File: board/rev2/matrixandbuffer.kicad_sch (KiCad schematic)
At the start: 2 parts, among them J4 Conn_02x08_Counter_Clockwise, U12 74HC245

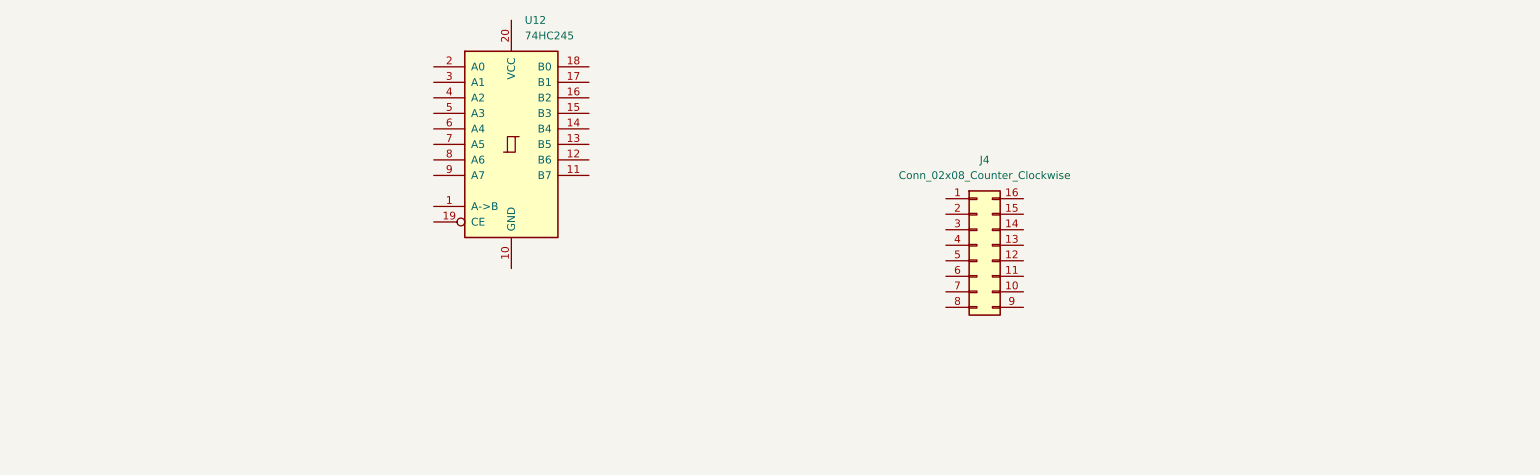
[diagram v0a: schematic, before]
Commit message: Continue board work
- move to rp2040, separate stm32g071 to do usb-c + aux ctrl IO
  - still cheaper lol with the cost of stm32s
- more power reg stuff
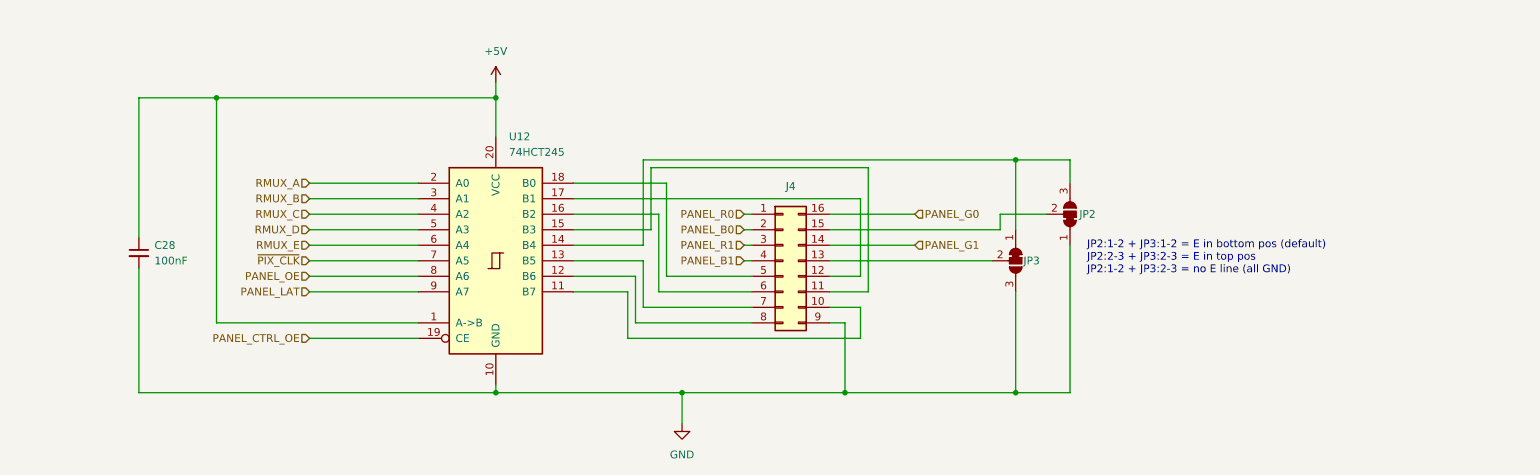
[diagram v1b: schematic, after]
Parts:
- added C28: 100nF, symbol Device:C_Small
- added JP2, JP3: SolderJumper_3_Bridged12, symbol Jumper:SolderJumper_3_Bridged12
- U12: value 74HC245 -> 74HCT245
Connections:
- net +5V: now reaches U12.1 (A->B)
- net +5V: now also U12.20 (VCC), C28.1
- net GND: now reaches U12.10 (GND)
- net GND: now also J4.9 (Pin_9), C28.2, JP2.1 (A), JP3.3 (B)
- net at U12.11 (B7): now also J4.10 (Pin_10)
- net at U12.12 (B6): now also J4.8 (Pin_8)
- net at U12.13 (B5): now also J4.7 (Pin_7)
- net at U12.14 (B4): now also JP2.3 (B), JP3.1 (A)
- net at U12.15 (B3): now also J4.11 (Pin_11)
- net at U12.16 (B2): now also J4.6 (Pin_6)
- net at U12.17 (B1): now also J4.12 (Pin_12)
- net at U12.18 (B0): now also J4.5 (Pin_5)
- net PANEL_CTRL_OE: now reaches U12.19 (CE)
- net RMUX_A: now reaches U12.2 (A0)
- net RMUX_B: now reaches U12.3 (A1)
- net RMUX_C: now reaches U12.4 (A2)
- net RMUX_D: now reaches U12.5 (A3)
- net RMUX_E: now reaches U12.6 (A4)
- net ~{PIX_CLK}: now reaches U12.7 (A5)
- net PANEL_OE: now reaches U12.8 (A6)
- net PANEL_LAT: now reaches U12.9 (A7)
- net PANEL_R0: now reaches J4.1 (Pin_1)
- net at J4.13 (Pin_13): now also JP3.2 (C)
- net PANEL_G1: now reaches J4.14 (Pin_14)
- net at J4.15 (Pin_15): now also JP2.2 (C)
- net PANEL_G0: now reaches J4.16 (Pin_16)
- net PANEL_B0: now reaches J4.2 (Pin_2)
- net PANEL_R1: now reaches J4.3 (Pin_3)
- net PANEL_B1: now reaches J4.4 (Pin_4)
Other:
- note added: "JP2:1-2 + JP3:1-2 = E in bottom pos (default) JP2:2-3 + JP3:2-3 = E in top pos JP2:1-2 + JP3:2-3 = no E line (all GND)"
- moved on the sheet: J4, U12

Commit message: Split out board into A/B
allow 2x displays (for chaining)
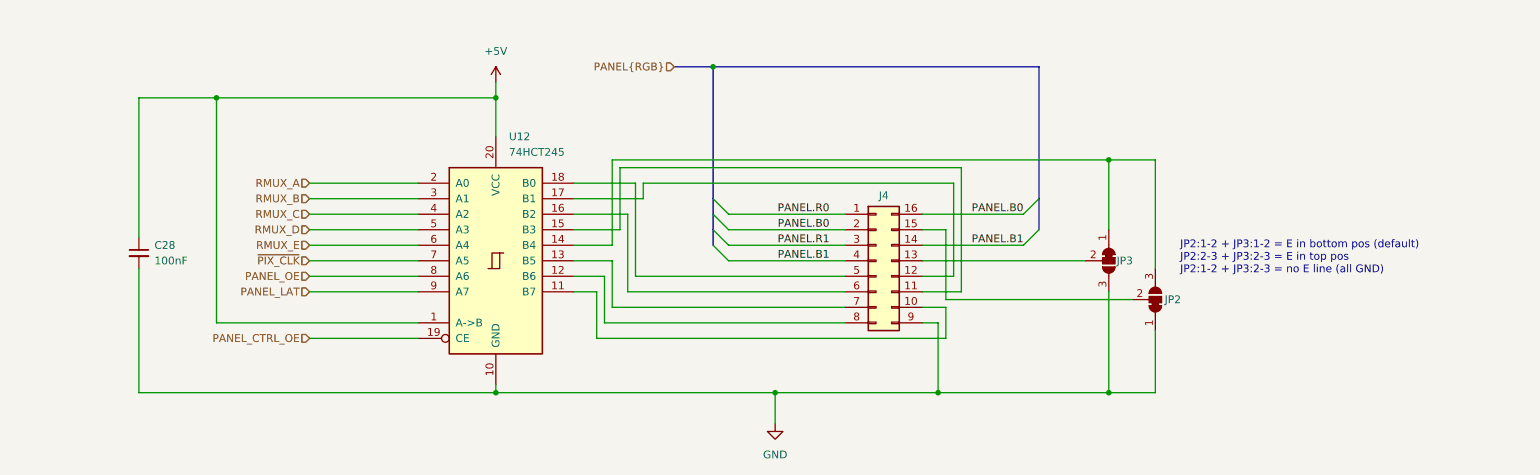
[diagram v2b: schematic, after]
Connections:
- net PANEL_G0 is gone; now on net PANEL.B0: J4.16 (Pin_16)
- net PANEL_G1 is gone; now on net PANEL.B1: J4.14 (Pin_14)
- net PANEL_B0 renamed PANEL.B0
- net PANEL_B1 renamed PANEL.B1
- net PANEL_R0 renamed PANEL.R0
- net PANEL_R1 renamed PANEL.R1
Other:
- moved on the sheet: J4, JP2, JP3

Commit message: More board work
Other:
- note removed: "JP2:1-2 + JP3:1-2 = E in bottom pos (default) JP2:2-3 + JP3:2-3 = E in top pos JP2:1-2 + JP3:2-3 = no E line (all GND)"
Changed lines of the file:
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@@
 	(generator_version "9.0")
 	(paper "A4")
-	(text "JP2:1-2 + JP3:1-2 = E in bottom pos (default)\nJP2:2-3 + JP3:2-3 = E in top pos\nJP2:1-2 + JP3:2-3 = no E line (all GND)"
-		(exclude_from_sim no)
-		(at 228.854 98.552 0)
-		(effects
-			(font
-				(size 1.27 1.27)
-			)
-			(justify left)
-		)
-	)
 	(junction
 		(at 162.56 120.65)
@@
 		)
 	)
+	(table
+		(column_count 3)
+		(border
+			(external yes)
+			(header yes)
+			(stroke
+				(width 0)
+				(type solid)
+			)
+		)
+		(separators
+			(rows no)
+			(cols yes)
+			(stroke
+				(width 0)
+				(type solid)
+			)
+		)
+		(column_widths 12.7 10.16 20.32)
+		(row_heights 2.54 2.54 2.54 2.54)
+		(cells
+			(table_cell "JP2"
+				(exclude_from_sim no)
+				(at 232.41 96.52 0)
+				(size 12.7 2.54)
+				(margins 0.9525 0.9525 0.9525 0.9525)
+				(span 1 1)
+				(fill
+					(type none)
+				)
+				(effects
+					(font
+						(size 1.27 1.27)
+						(thickness 0.254)
+						(bold yes)
+					)
+					(justify top)
+				)
+			)
+			(table_cell "JP3"
+				(exclude_from_sim no)
+				(at 245.11 96.52 0)
+				(size 10.16 2.54)
+				(margins 0.9525 0.9525 0.9525 0.9525)
+				(span 1 1)
+				(fill
+					(type none)
+				)
+				(effects
+					(font
+						(size 1.27 1.27)
+						(thickness 0.254)
+						(bold yes)
+					)
+					(justify top)
+				)
+			)
+			(table_cell ""
+				(exclude_from_sim no)
+				(at 255.27 96.52 0)
+				(size 20.32 2.54)
+				(margins 0.9525 0.9525 0.9525 0.9525)
+				(span 1 1)
+				(fill
+					(type color)
+					(color 255 255 194 1)
+				)
+				(effects
+					(font
+						(size 1.27 1.27)
+					)
+					(justify left top)
+				)
+			)
+			(table_cell "default"
+				(exclude_from_sim no)
+				(at 232.41 99.06 0)
+				(size 12.7 2.54)
+				(margins 0.9525 0.9525 0.9525 0.9525)
+				(span 1 1)
+				(fill
+					(type none)
+				)
+				(effects
+					(font
+						(size 1.27 1.27)
+					)
+					(justify left top)
+				)
+			)
+			(table_cell "default"
+				(exclude_from_sim no)
+				(at 245.11 99.06 0)
+				(size 10.16 2.54)
+				(margins 0.9525 0.9525 0.9525 0.9525)
+				(span 1 1)
+				(fill
+					(type none)
+				)
+				(effects
+					(font
+						(size 1.27 1.27)
+					)
+					(justify left top)
+				)
+			)
+			(table_cell "E on bottom"
+				(exclude_from_sim no)
+				(at 255.27 99.06 0)
+				(size 20.32 2.54)
+				(margins 0.9525 0.9525 0.9525 0.9525)
+				(span 1 1)
+				(fill
+					(type none)
+				)
+				(effects
+					(font
+						(size 1.27 1.27)
+					)
+					(justify left top)
+				)
+			)
+			(table_cell "cut"
+				(exclude_from_sim no)
+				(at 232.41 101.6 0)
+				(size 12.7 2.54)
+				(margins 0.9525 0.9525 0.9525 0.9525)
+				(span 1 1)
+				(fill
+					(type none)
+				)
+				(effects
+					(font
+						(size 1.27 1.27)
+					)
+					(justify left top)
+				)
+			)
+			(table_cell "cut"
+				(exclude_from_sim no)
+				(at 245.11 101.6 0)
+				(size 10.16 2.54)
+				(margins 0.9525 0.9525 0.9525 0.9525)
+				(span 1 1)
+				(fill
+					(type none)
+				)
+				(effects
+					(font
+						(size 1.27 1.27)
+					)
+					(justify left top)
+				)
+			)
+			(table_cell "E on top"
+				(exclude_from_sim no)
+				(at 255.27 101.6 0)
+				(size 20.32 2.54)
+				(margins 0.9525 0.9525 0.9525 0.9525)
+				(span 1 1)
+				(fill
+					(type none)
+				)
+				(effects
+					(font
+						(size 1.27 1.27)
+					)
+					(justify left top)
+				)
+			)
+			(table_cell "default"
+				(exclude_from_sim no)
+				(at 232.41 104.14 0)
+				(size 12.7 2.54)
+				(margins 0.9525 0.9525 0.9525 0.9525)
+				(span 1 1)
+				(fill
+					(type none)
+				)
+				(effects
+					(font
+						(size 1.27 1.27)
+					)
+					(justify left top)
+				)
+			)
+			(table_cell "cut"
+				(exclude_from_sim no)
+				(at 245.11 104.14 0)
+				(size 10.16 2.54)
+				(margins 0.9525 0.9525 0.9525 0.9525)
+				(span 1 1)
+				(fill
+					(type none)
+				)
+				(effects
+					(font
+						(size 1.27 1.27)
+					)
+					(justify left top)
+				)
+			)
+			(table_cell "both choices GND"
+				(exclude_from_sim no)
+				(at 255.27 104.14 0)
+				(size 20.32 2.54)
+				(margins 0.9525 0.9525 0.9525 0.9525)
+				(span 1 1)
+				(fill
+					(type none)
+				)
+				(effects
+					(font
+						(size 1.27 1.27)
+					)
+					(justify left top)
+				)
+			)
+		)
+	)

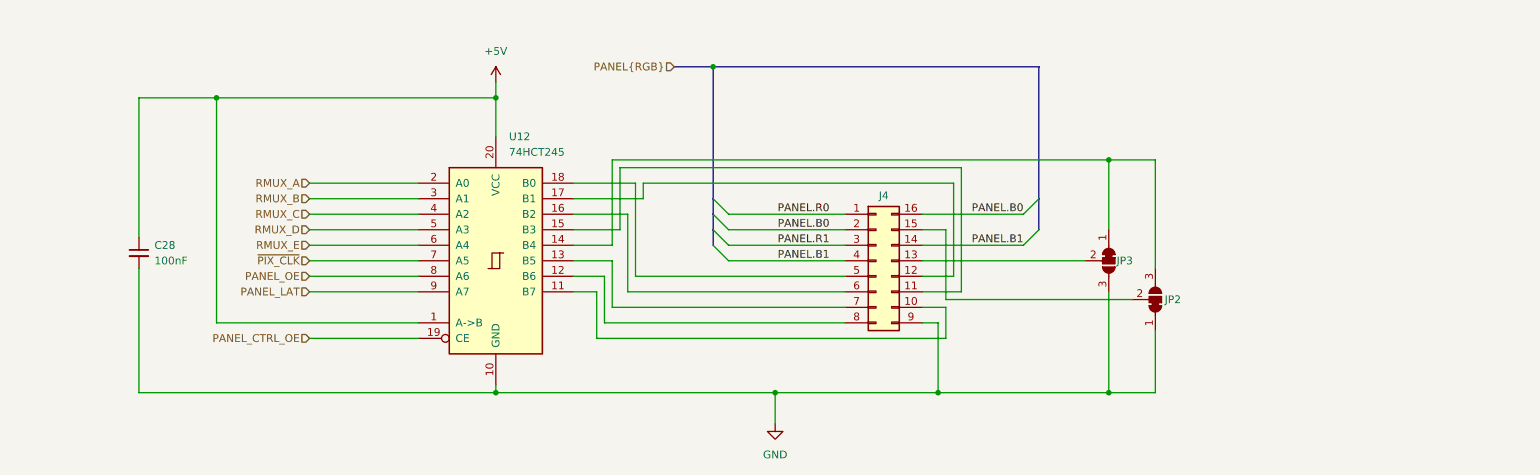
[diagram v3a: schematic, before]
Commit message: Board GPIO allocation
- and usbmux

still need to do termination on the big buses + a bunch of bypass caps
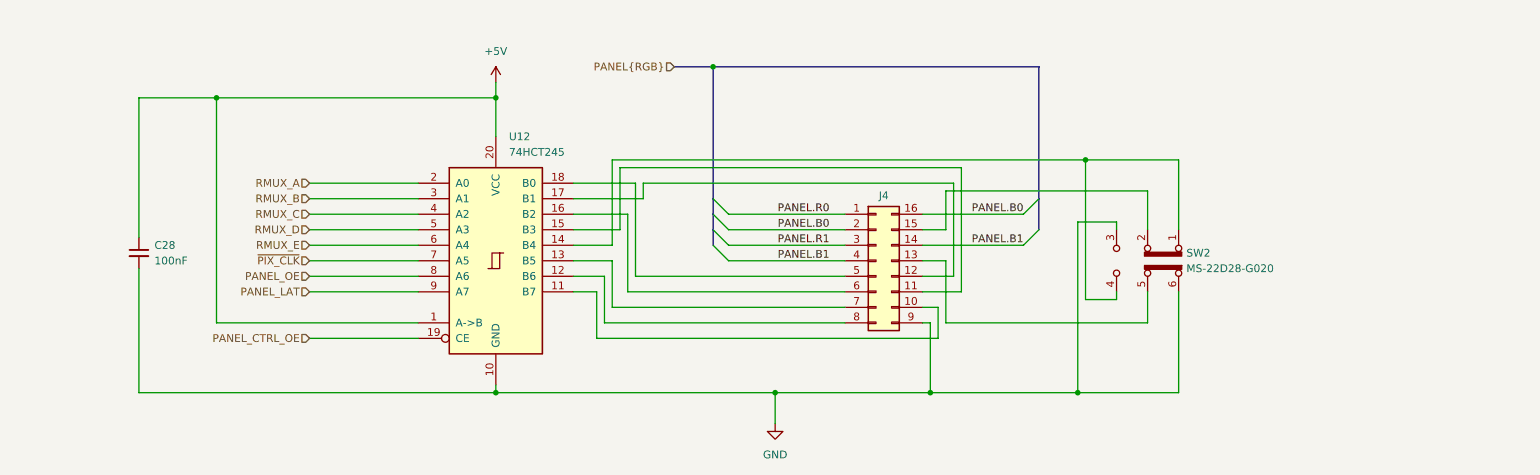
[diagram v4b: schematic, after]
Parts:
- removed JP2, JP3: SolderJumper_3_Bridged12, symbol Jumper:SolderJumper_3_Bridged12
- added SW2: MS-22D28-G020, symbol Switch:SW_Slide_DPDT
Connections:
- net GND: now also SW2.3 (C), SW2.6 (C)
- net at J4.15 (Pin_15): now also SW2.2 (B)
- net at U12.14 (B4): now also SW2.1 (A), SW2.4 (A)
- net at J4.13 (Pin_13): now also SW2.5 (B)
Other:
- company: (none) -> MLABS
- title: (none) -> LED Level Shifter + Socket

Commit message: Continue board, assign caps/res, adjust for JLC availability
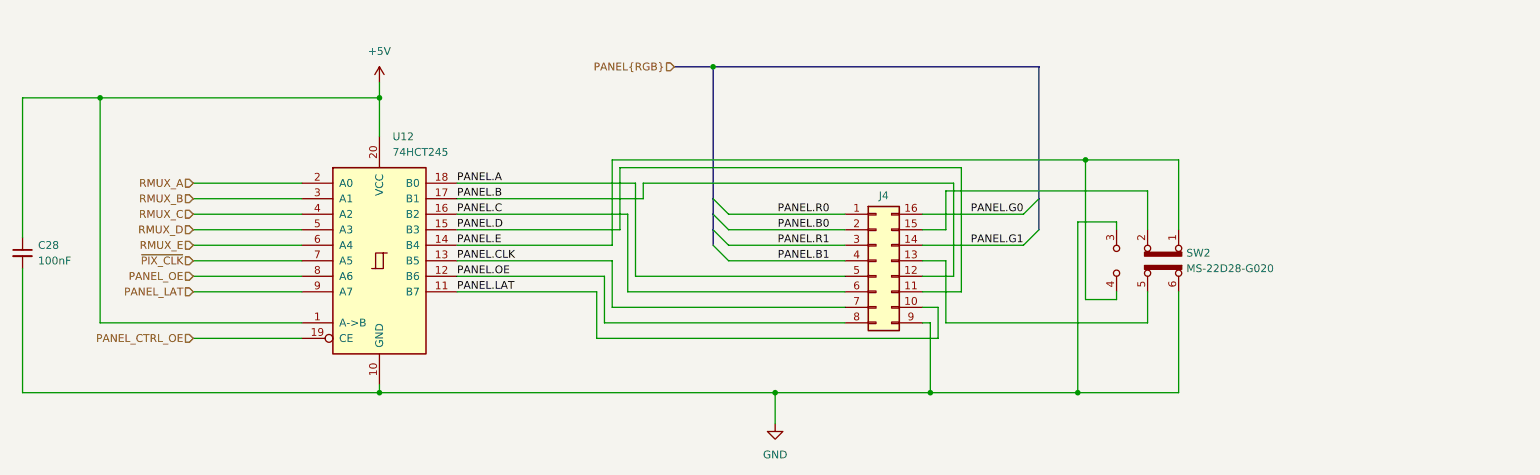
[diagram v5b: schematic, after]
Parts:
- C28: footprint (none) -> Capacitor_SMD:C_0402_1005Metric; Part (none) -> CL05B104KB54PNC
- J4: footprint (none) -> Connector_IDC:IDC-Header_2x07_P2.54mm_Vertical
- U12: footprint (none) -> Package_SO:TSSOP-20-1EP_4.4x6.5mm_P0.65mm_EP2.15x3.35mm
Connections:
- net PANEL.B0: no longer J4.16 (Pin_16)
- net PANEL.B1: no longer J4.14 (Pin_14)
- net PANEL.LAT: now reaches J4.10 (Pin_10), U12.11 (B7)
- net PANEL.OE: now reaches J4.8 (Pin_8), U12.12 (B6)
- net PANEL.CLK: now reaches J4.7 (Pin_7), U12.13 (B5)
- net PANEL.E: now reaches SW2.1 (A), SW2.4 (A), U12.14 (B4)
- net PANEL.D: now reaches J4.11 (Pin_11), U12.15 (B3)
- net PANEL.C: now reaches J4.6 (Pin_6), U12.16 (B2)
- net PANEL.B: now reaches J4.12 (Pin_12), U12.17 (B1)
- net PANEL.A: now reaches J4.5 (Pin_5), U12.18 (B0)
- new net PANEL.G0: J4.16 (Pin_16)
- new net PANEL.G1: J4.14 (Pin_14)
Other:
- moved on the sheet: C28, U12

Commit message: Start new PCB
- all footprints setup
- need to setup netclasses next, tho
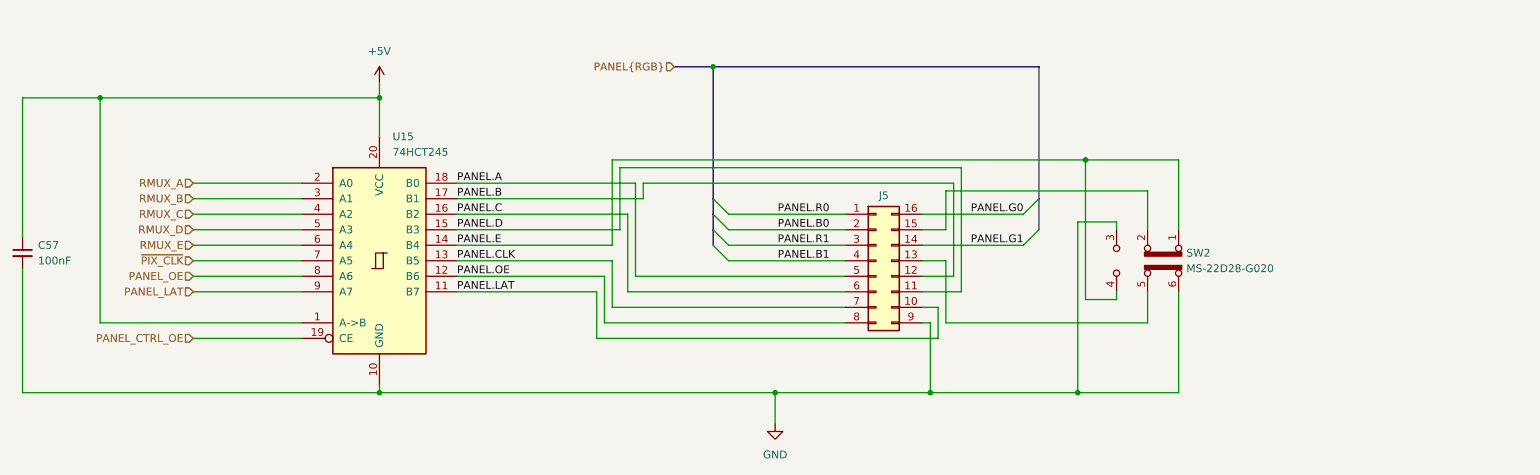
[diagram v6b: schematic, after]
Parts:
- J5: renamed from J4; footprint Connector_IDC:IDC-Header_2x07_P2.54mm_Vertical -> Connector_IDC:IDC-Header_2x08_P2.54mm_Vertical
- SW2: footprint (none) -> Switch_Slide_SMD:SW-SMD_MS-22D28-G020; Part (none) -> MS-22D28-G020
- U15: renamed from U12; Part (none) -> 74HCT245
- renumbered C28 to C57
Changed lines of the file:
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@@
 		(dnp no)
 		(fields_autoplaced yes)
-		(property "Reference" "U12"
+		(property "Reference" "U15"
 			(at 99.9333 78.74 0)
 			(effects
@@
 					(size 1.27 1.27)
 					(color 255 255 194 1)
+				)
+				(hide yes)
+			)
+		)
+		(property "Part" "74HCT245"
+			(at 97.79 99.06 0)
+			(effects
+				(font
+					(size 1.27 1.27)
 				)
 				(hide yes)
@@
 			(project "mainboard"
 				(path "/32eb05c7-b4a6-42f3-8fb3-43453631100f/b5a611d3-6308-4792-ad5f-d479afbae4ce"
-					(reference "U12")
+					(reference "U15")
 					(unit 1)
 				)
 				(path "/32eb05c7-b4a6-42f3-8fb3-43453631100f/e7e17249-2796-40aa-8cf6-7a1737723276"
-					(reference "U17")
+					(reference "U16")
 					(unit 1)
 				)
@@
 		(dnp no)
 		(fields_autoplaced yes)
-		(property "Reference" "C28"
+		(property "Reference" "C57"
 			(at 41.91 96.5262 0)
 			(effects
@@
 			(project "mainboard"
 				(path "/32eb05c7-b4a6-42f3-8fb3-43453631100f/b5a611d3-6308-4792-ad5f-d479afbae4ce"
-					(reference "C28")
+					(reference "C57")
 					(unit 1)
 				)
 				(path "/32eb05c7-b4a6-42f3-8fb3-43453631100f/e7e17249-2796-40aa-8cf6-7a1737723276"
-					(reference "C35")
+					(reference "C58")
 					(unit 1)
 				)
@@
 		(dnp no)
 		(fields_autoplaced yes)
-		(property "Reference" "#PWR0102"
+		(property "Reference" "#PWR045"
 			(at 97.79 73.66 0)
 			(effects
@@
 			(project "mainboard"
 				(path "/32eb05c7-b4a6-42f3-8fb3-43453631100f/b5a611d3-6308-4792-ad5f-d479afbae4ce"
-					(reference "#PWR0102")
+					(reference "#PWR045")
 					(unit 1)
 				)
 				(path "/32eb05c7-b4a6-42f3-8fb3-43453631100f/e7e17249-2796-40aa-8cf6-7a1737723276"
-					(reference "#PWR036")
+					(reference "#PWR047")
 					(unit 1)
 				)
@@
 			)
 		)
-		(property "Footprint" ""
+		(property "Footprint" "Switch_Slide_SMD:SW-SMD_MS-22D28-G020"
 			(at 228.6 113.03 0)
 			(effects
@@
 		(property "Description" "Slide Switch, dual pole double throw"
 			(at 223.52 99.06 0)
+			(effects
+				(font
+					(size 1.27 1.27)
+				)
+				(hide yes)
+			)
+		)
+		(property "Part" "MS-22D28-G020"
+			(at 223.52 99.06 90)
 			(effects
 				(font
@@
 		(on_board yes)
 		(dnp no)
-		(property "Reference" "J4"
+		(property "Reference" "J5"
 			(at 180.34 88.392 0)
 			(effects
@@
 			)
 		)
-		(property "Footprint" "Connector_IDC:IDC-Header_2x07_P2.54mm_Vertical"
+		(property "Footprint" "Connector_IDC:IDC-Header_2x08_P2.54mm_Vertical"
 			(at 179.07 99.06 0)
 			(effects
@@
 			(project "mainboard"
 				(path "/32eb05c7-b4a6-42f3-8fb3-43453631100f/b5a611d3-6308-4792-ad5f-d479afbae4ce"
-					(reference "J4")
+					(reference "J5")
 					(unit 1)
 				)
 				(path "/32eb05c7-b4a6-42f3-8fb3-43453631100f/e7e17249-2796-40aa-8cf6-7a1737723276"
-					(reference "J5")
+					(reference "J6")
 					(unit 1)
 				)
@@
 		(dnp no)
 		(fields_autoplaced yes)
-		(property "Reference" "#PWR0101"
+		(property "Reference" "#PWR046"
 			(at 162.56 132.08 0)
 			(effects
@@
 			(project "mainboard"
 				(path "/32eb05c7-b4a6-42f3-8fb3-43453631100f/b5a611d3-6308-4792-ad5f-d479afbae4ce"
-					(reference "#PWR0101")
+					(reference "#PWR046")
 					(unit 1)
 				)
 				(path "/32eb05c7-b4a6-42f3-8fb3-43453631100f/e7e17249-2796-40aa-8cf6-7a1737723276"
-					(reference "#PWR037")
-					(unit 1)
-				)
+					(reference "#PWR048")
+					(unit 1)
+				)
